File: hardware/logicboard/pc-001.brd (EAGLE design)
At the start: 25 x 61.5 mm, 17 parts, among them J4 DNP, J5 DNP

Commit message: Rerouted.
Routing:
- net GND: track 82.0 -> 62.5 mm, vias 1 -> 3
- net A6: track 77.1 -> 57.8 mm, vias 0 -> 2
- net A4: track 52.9 -> 36.4 mm, vias 4 -> 3
- net A0: track 52.6 -> 40.3 mm
- net D2: track 27.4 -> 39.0 mm
- net D7: track 29.4 -> 23.5 mm
- net SDA: track 28.0 -> 33.8 mm, vias 2 -> 0
- net VCC: track 90.7 -> 87.2 mm
- net D3: track 36.9 -> 34.2 mm, vias 2 -> 0
- net A1: track 27.8 -> 30.0 mm, vias 1 -> 0
- net A5: track 57.3 -> 55.4 mm

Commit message: Route update.
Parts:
- moved LOGO1 0.50 mm to (12.5, 2.50)
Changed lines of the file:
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@@
 <attribute name="VALUE" x="20.12" y="12.268" size="0.6096" layer="28" font="vector" ratio="20" rot="MR0"/>
 </element>
-<element name="LOGO1" library="SparkFun-Aesthetics" package="OSHW-LOGO-S_COPPER" value="OSHW-LOGOS-COPPER" x="12.5" y="2"/>
+<element name="LOGO1" library="SparkFun-Aesthetics" package="OSHW-LOGO-S_COPPER" value="OSHW-LOGOS-COPPER" x="12.5" y="2.5"/>
 <element name="U$1" library="pineapple" package="PINEAPPLE450" value="PINEAPPLE450" x="12.5" y="56"/>
 </elements>
@@
 <via x="12.6492" y="40.6908" extent="1-16" drill="0.3"/>
 <via x="14.1732" y="39.1668" extent="1-16" drill="0.3"/>
-<polygon width="0.254" layer="1">
+<polygon width="0.127" layer="1">
 <vertex x="-1" y="-1"/>
 <vertex x="26" y="-1"/>
@@
 <vertex x="-1" y="62"/>
 </polygon>
-<polygon width="0.254" layer="16">
+<polygon width="0.127" layer="16">
 <vertex x="-2" y="-2"/>
 <vertex x="27" y="-2"/>

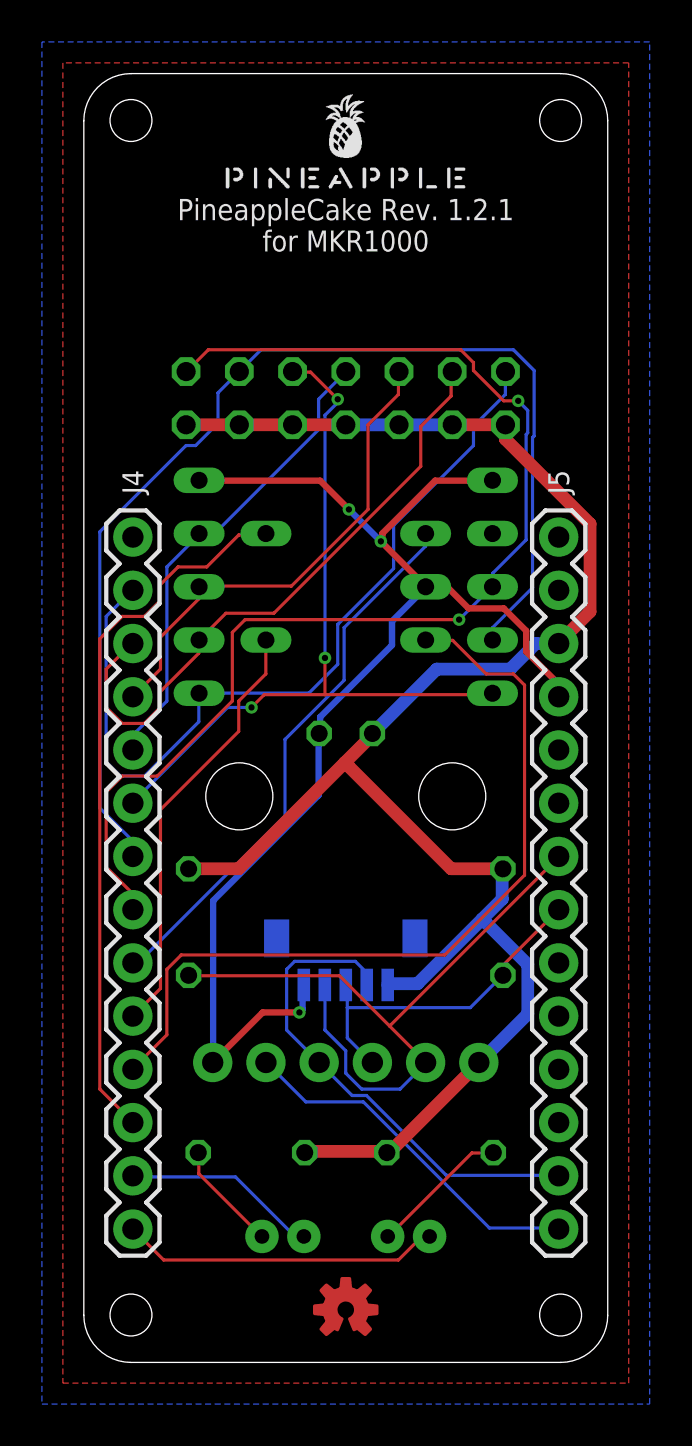
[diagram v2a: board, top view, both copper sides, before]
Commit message: 1st pin of I2C connector now has 5V supply, not 3.3V.
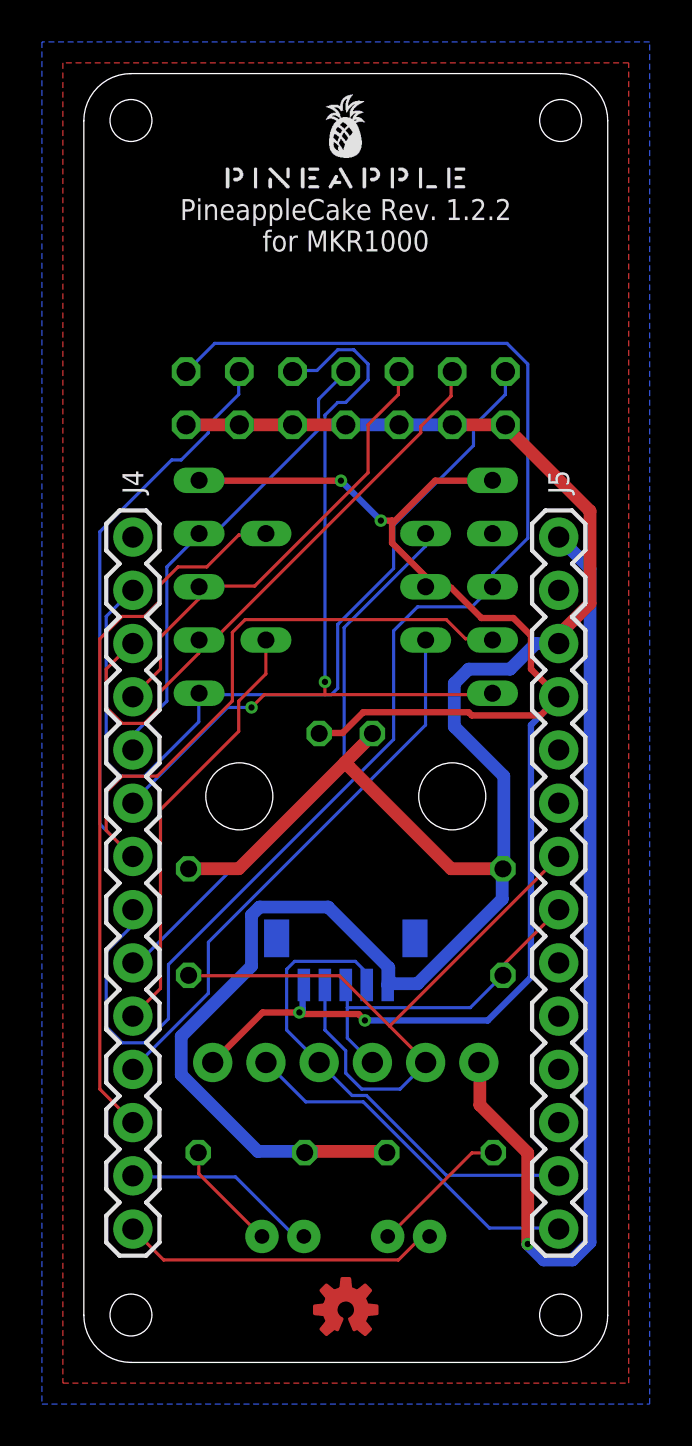
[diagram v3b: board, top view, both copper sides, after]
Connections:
- new net +5V: J5.14, MMA8452Q.1
- net VCC: no longer MMA8452Q.1
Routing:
- net +5V: track 0.00 -> 47.5 mm, vias 0 -> 1
- net VCC: track 87.2 -> 102.5 mm
- net D2: track 39.0 -> 26.3 mm
- net GND: track 62.5 -> 73.7 mm, vias 3 -> 4
- net A6: track 57.8 -> 67.0 mm, vias 2 -> 0
- net A4: track 36.4 -> 40.5 mm, vias 3 -> 2
- net A2: track 23.3 -> 22.3 mm
- net A1: track 30.0 -> 29.0 mm
- net A5: track 55.4 -> 54.6 mm
- net A0: track 40.3 -> 41.1 mm
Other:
- board text added: "PineappleCake Rev. 1.2.2"
- board text removed: "PineappleCake Rev. 1.2.1"

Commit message: Hotfix. I2C connector is now connected to +5V, not +3.3V (Vcc).
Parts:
- I2C: value 3.3V -> (none)
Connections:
- net +5V: now also I2C.1
- net VCC: no longer I2C.1
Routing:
- net A6: track 67.0 -> 57.6 mm, vias 0 -> 2
- net VCC: track 102.5 -> 96.2 mm
- net +5V: track 47.5 -> 42.0 mm, vias 1 -> 3
- net GND: track 73.7 -> 78.4 mm, vias 4 -> 3
- net A4: track 40.5 -> 36.2 mm, vias 2 -> 3
- net D2: track 26.3 -> 29.7 mm, vias 0 -> 1
- net A5: track 54.6 -> 55.4 mm
- net D0: track 26.4 -> 27.0 mm
- net A0: track 41.1 -> 40.5 mm

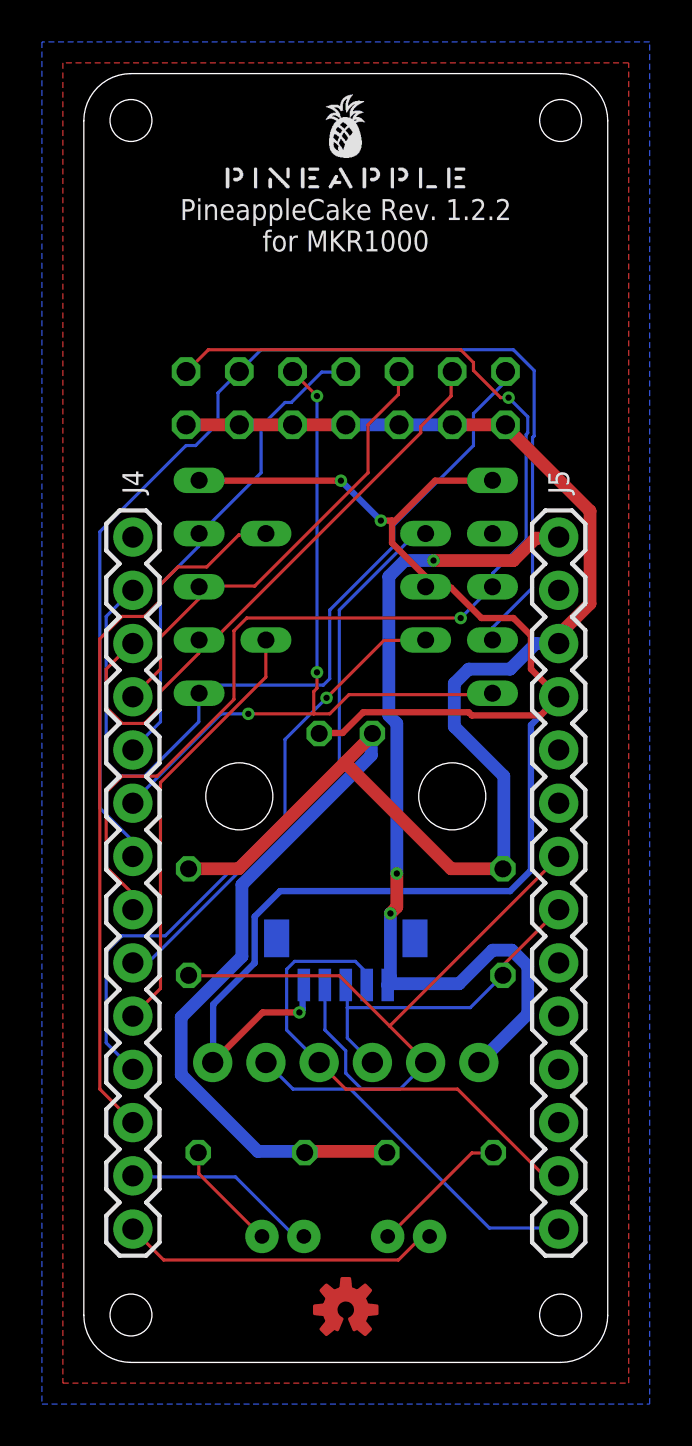
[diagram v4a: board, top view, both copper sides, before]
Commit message: Fixed wrong connection to MMA8452Q.
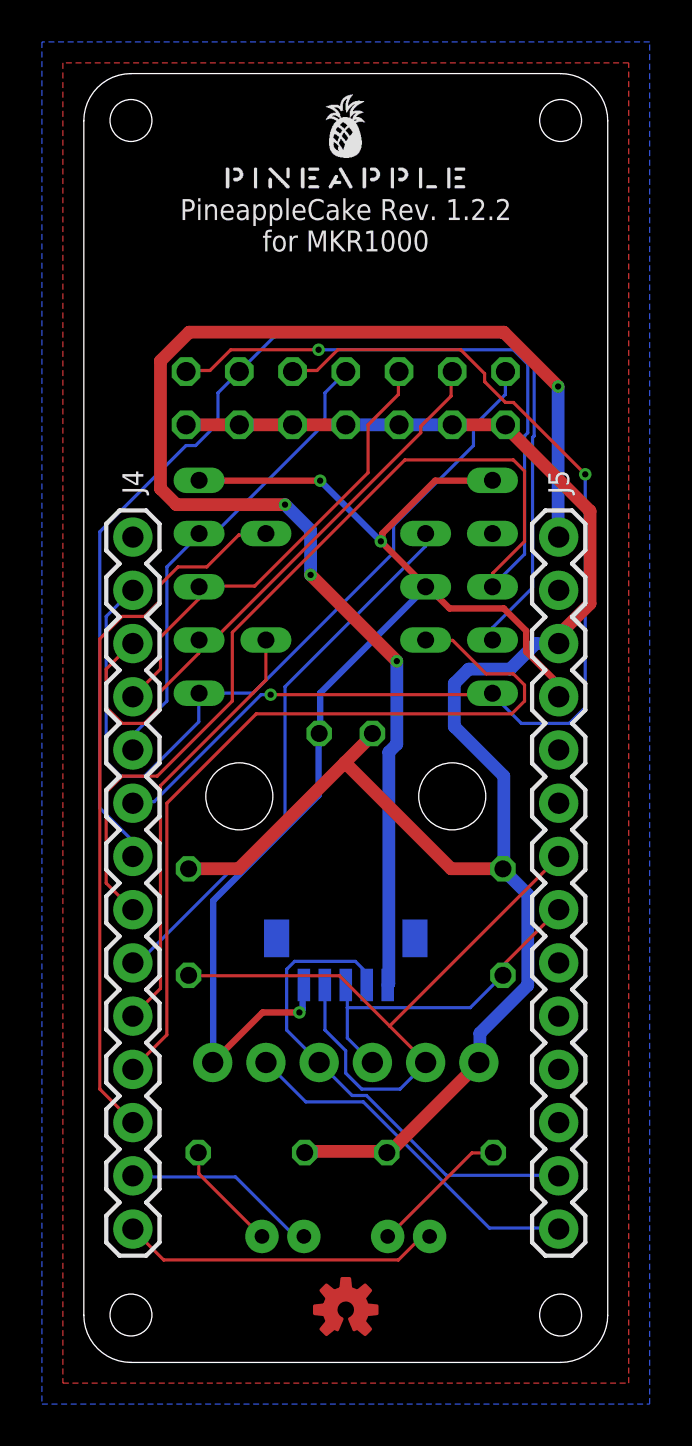
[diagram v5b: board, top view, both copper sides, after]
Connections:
- net +5V: no longer MMA8452Q.1
- net VCC: now also MMA8452Q.1
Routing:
- net +5V: track 42.0 -> 65.5 mm, vias 3 -> 4
- net A4: track 36.2 -> 53.0 mm, vias 3 -> 2
- net GND: track 78.4 -> 62.5 mm
- net A6: track 57.6 -> 69.3 mm, vias 2 -> 1
- net VCC: track 96.2 -> 85.5 mm
- net D2: track 29.7 -> 38.8 mm, vias 1 -> 0
- net A0: track 40.5 -> 38.8 mm
- net A5: track 55.4 -> 56.2 mm
- net D0: track 27.0 -> 26.4 mm

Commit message: Fixed positioning of MMA8452Q.
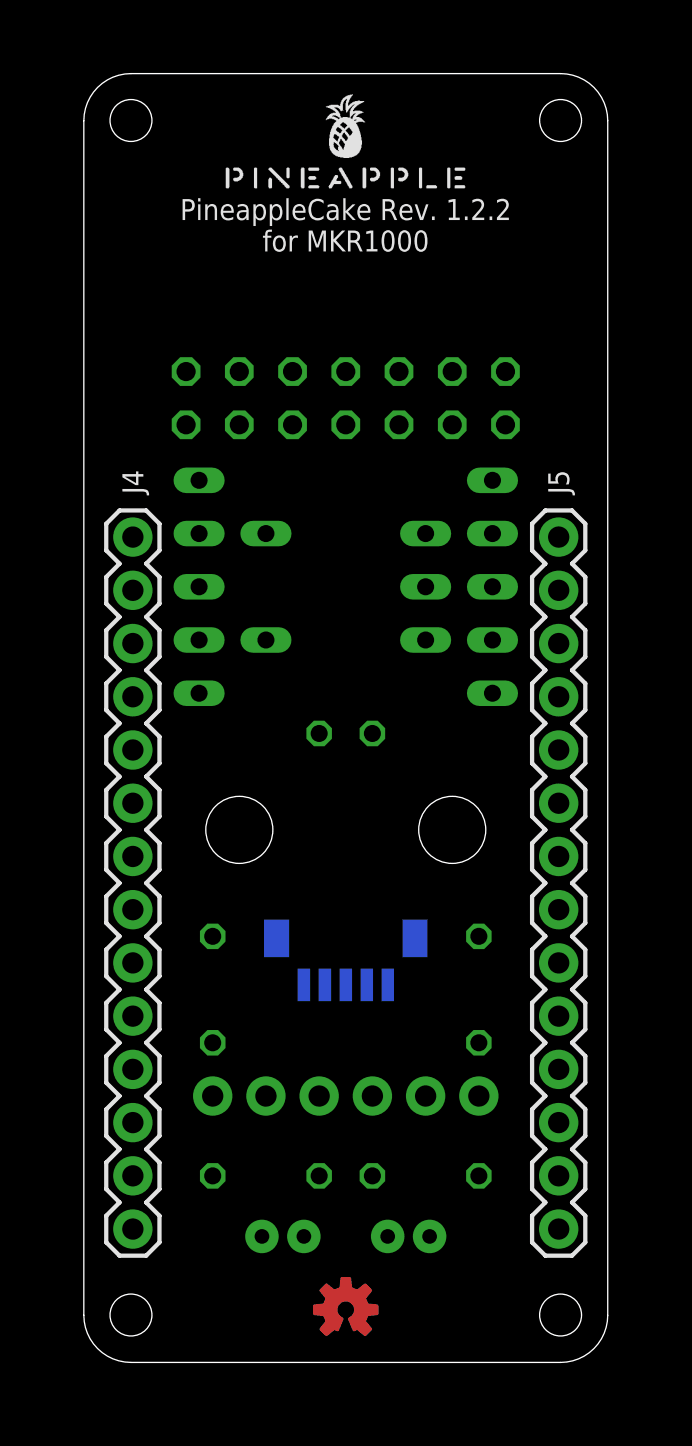
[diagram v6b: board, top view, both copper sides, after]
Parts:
- moved R3 3.42 mm to (6.15, 17.8)
- moved R4 3.42 mm to (18.9, 17.8)
- moved MMA8452Q 1.60 mm to (18.9, 12.7)
- moved R2 1.31 mm to (16.3, 8.89)
- moved R1 1.31 mm to (8.69, 8.89)
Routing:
- net VCC: track 85.5 -> 0.00 mm
- net A6: track 69.3 -> 0.00 mm, vias 1 -> 0
- net +5V: track 65.5 -> 0.00 mm, vias 4 -> 0
- net GND: track 62.5 -> 0.00 mm, vias 3 -> 0
- net A5: track 56.2 -> 0.00 mm
- net A4: track 53.0 -> 0.00 mm, vias 2 -> 0
- net D2: track 38.8 -> 0.00 mm
- net A0: track 38.8 -> 0.00 mm
- net D3: track 34.2 -> 0.00 mm
- net SDA: track 33.8 -> 0.00 mm
- net A1: track 29.0 -> 0.00 mm
- net D0: track 26.4 -> 0.00 mm
- net D7: track 23.5 -> 0.00 mm
- net A3: track 22.7 -> 0.00 mm
- net A2: track 22.3 -> 0.00 mm
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- removed copper zone on layer 1, net GND
- removed copper zone on layer 16, net GND

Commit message: Fixed connection of SDA.
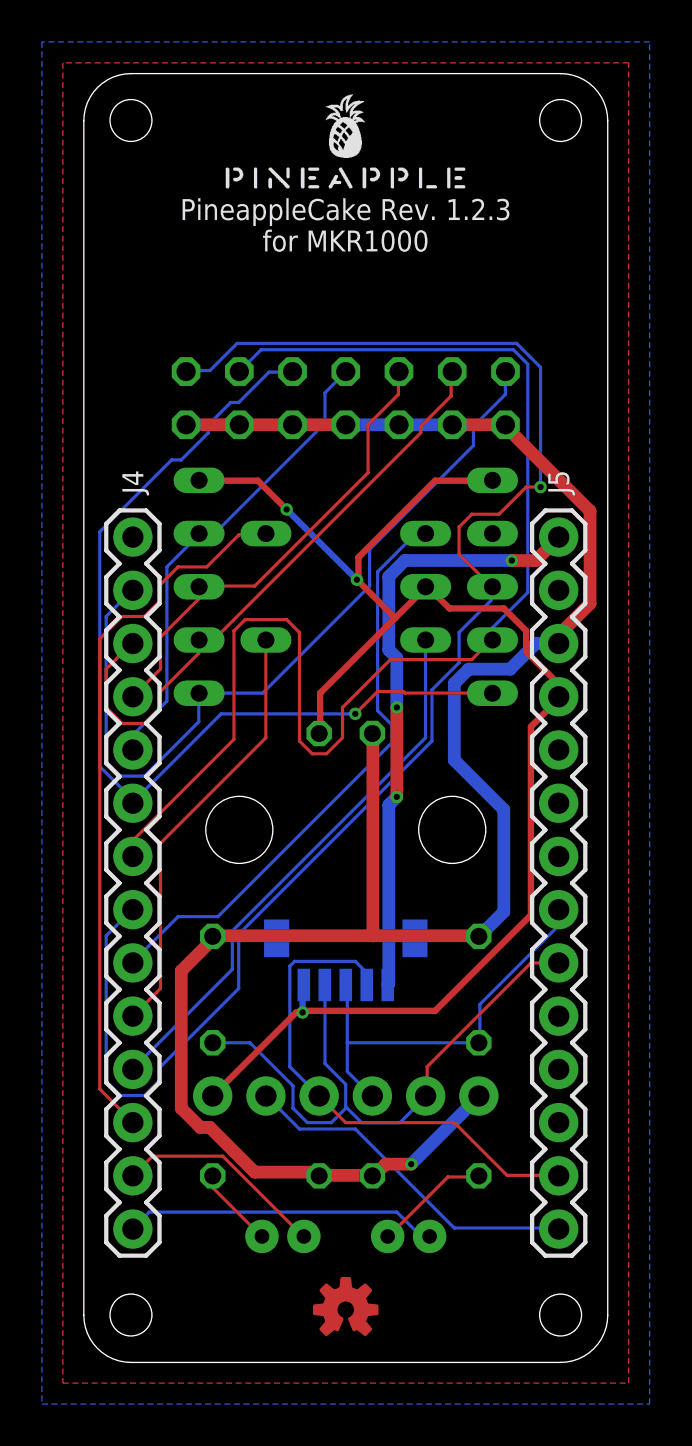
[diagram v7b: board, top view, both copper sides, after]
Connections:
- net SDA: now also J5.6; no longer J5.8
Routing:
- net VCC: track 0.00 -> 95.5 mm, vias 0 -> 1
- net A6: track 0.00 -> 73.9 mm, vias 0 -> 1
- net GND: track 0.00 -> 70.7 mm, vias 0 -> 3
- net A5: track 0.00 -> 62.4 mm
- net A4: track 0.00 -> 45.6 mm, vias 0 -> 1
- net A0: track 0.00 -> 39.0 mm
- net D3: track 0.00 -> 34.2 mm
- net SDA: track 0.00 -> 29.6 mm
- net A1: track 0.00 -> 29.0 mm
- net +5V: track 0.00 -> 28.7 mm, vias 0 -> 3
- net D0: track 0.00 -> 28.3 mm
- net D2: track 0.00 -> 26.3 mm
- net D7: track 0.00 -> 24.4 mm
- net A3: track 0.00 -> 22.7 mm
- net A2: track 0.00 -> 22.3 mm
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- added copper zone on layer 1, net GND
- added copper zone on layer 16, net GND
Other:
- board text added: "PineappleCake Rev. 1.2.3"
- board text removed: "PineappleCake Rev. 1.2.2"
